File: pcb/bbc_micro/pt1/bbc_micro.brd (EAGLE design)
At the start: 56 x 65 mm, 51 parts, among them IC1 STM32F072C8T6, SW1 324_SW, SW2 324_SW, SW3 324_SW

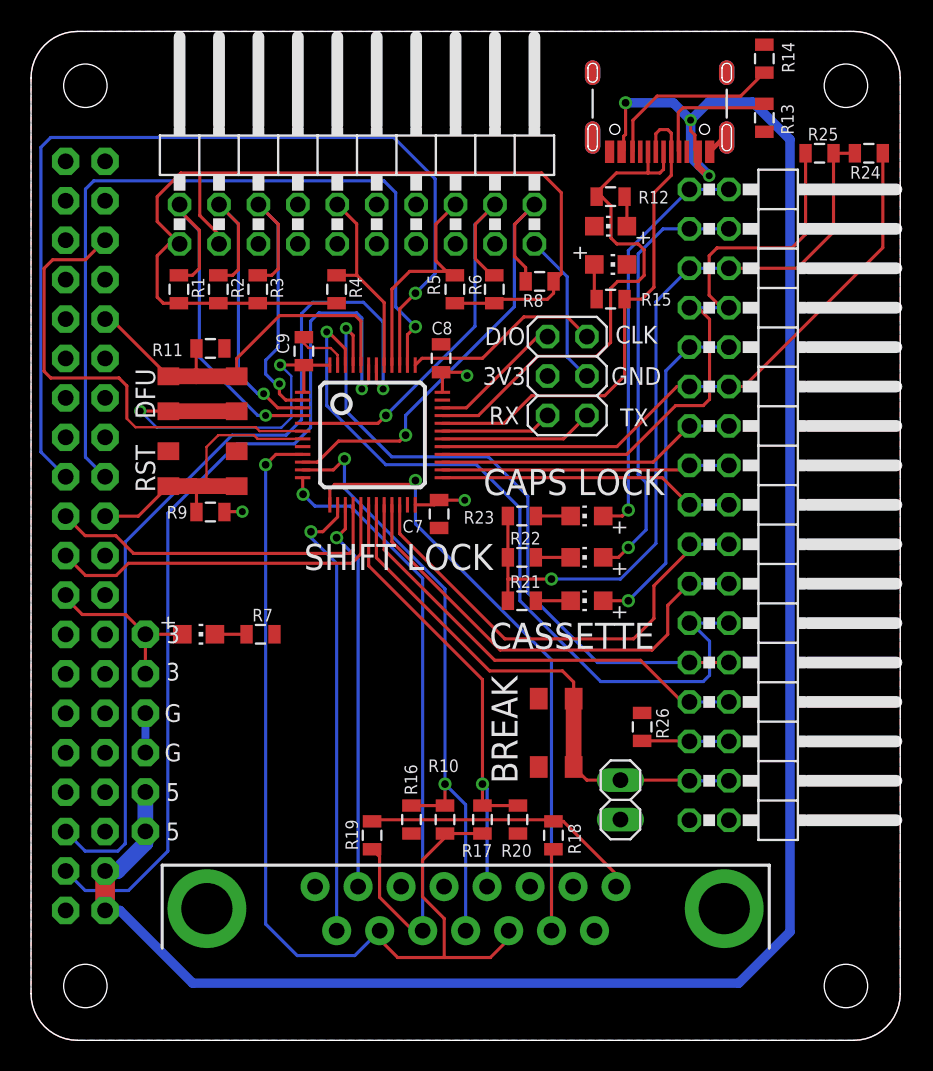
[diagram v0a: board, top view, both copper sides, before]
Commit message: changed to using built-in DAC
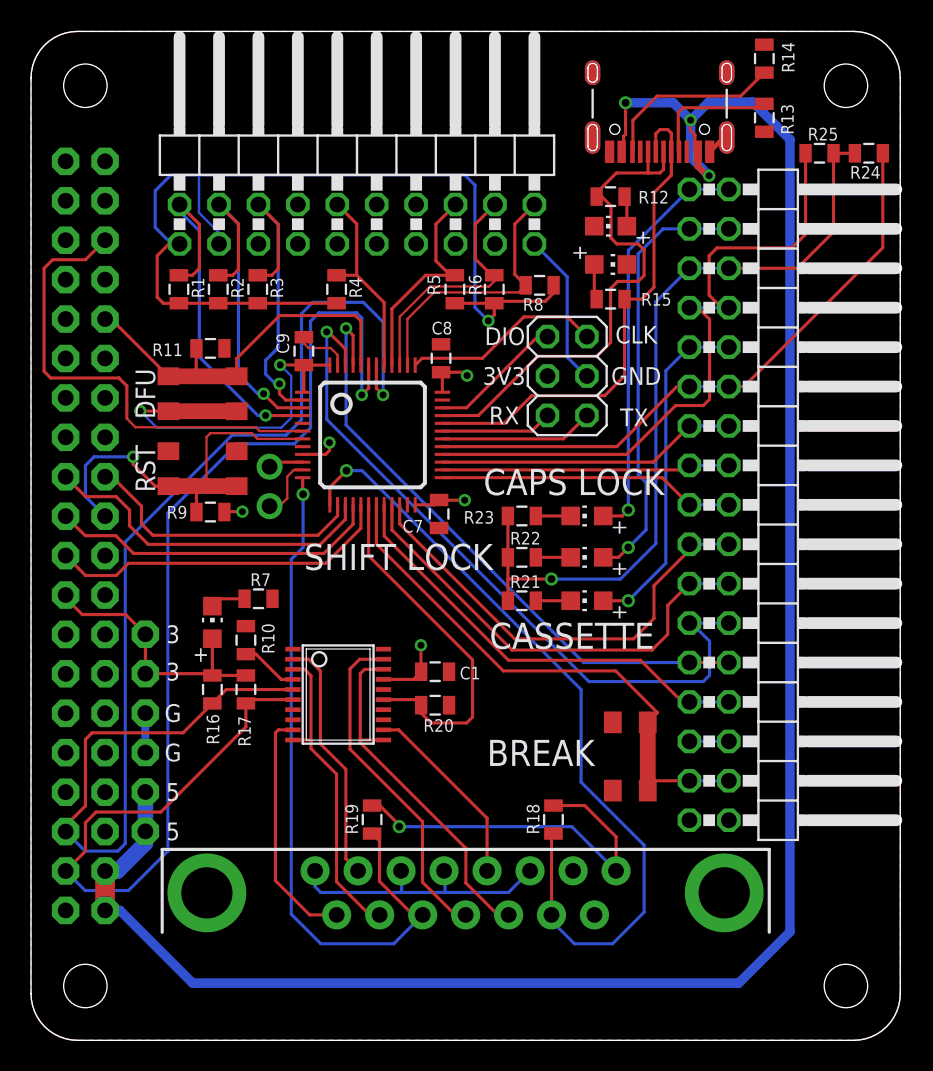
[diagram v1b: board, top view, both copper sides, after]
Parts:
- removed JP5: (no value), pinhead:1X02
- removed R26: 5.1K, SparkFun-Passives:0805
- added C1: 100nF, clock:0805@1
- added U$1: PINHD1X2, adafruit_changed:1X02
- added U$5: MCP4451, ps2:TSSOP20
- R10: value 5.1K -> 2K
- moved R17 17.4 mm to (13.8, 22.6)
- moved R10 17.3 mm to (13.8, 25.8)
- moved R16 15.3 mm to (11.7, 22.6), turned to 90 degrees
- moved R20 9.09 mm to (26.0, 21.6), turned to 0 degrees
- moved SW3 5.01 mm to (38.6, 18.3)
- moved R7 2.29 mm to (14.7, 28.4)
- moved LED1 1.17 mm to (11.7, 26.9), turned to 0 degrees
- moved R18 1.02 mm to (33.7, 14.2)
- moved R19 1.02 mm to (22.0, 14.2)
- moved U$9 1.02 mm to (28.0, 9.50)
- moved R8 0.25 mm to (32.8, 48.6)
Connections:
- removed net N$12 (its old number): IC1.18, R17.2, R20.1, U$9.4
- new net N$10: U$5.19, U$9.12
- new net N$19: U$5.11, U$5.18, U$9.11
- new net N$24: IC1.10, U$1.1
- new net N$25: IC1.18, R20.1, U$5.15
- new net N$31: IC1.11, U$1.2
- new net N$6: U$5.9, U$9.15
- net +3V3: now also C1.2, IC1.9, R16.2, R17.2, U$5.17
- net BREAK: no longer JP5.1
- net CLK: no longer R26.1
- net D6/MIDDLE: now also IC1.39; no longer IC1.5
- net D7/RIGHTT: now also IC1.38; no longer IC1.10
- net GND: now also C1.1, R10.2, U$5.16, U$5.7; no longer JP5.2, R16.2, R26.2
- net N$11: now also U$5.12, U$9.4; no longer IC1.9, R10.1, R17.1, U$9.11, U$9.14
- net N$17: now also U$5.10, U$5.3, U$9.14; no longer IC1.11, R10.2, R16.1, U$9.12
- net N$22: now also R16.1, U$5.5
- net N$23: now also R17.1, U$5.6
- net N$4: now also R10.1, U$5.4; no longer IC1.14, U$9.15
- net N$5: now also U$5.2; no longer IC1.15
- net SPI_CS: now also IC1.14; no longer IC1.38
- net SPI_SCK: now also IC1.15; no longer IC1.39
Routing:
- net N$11: track 63.1 -> 12.4 mm, vias 1 -> 0
- net SPI_SCK: track 61.6 -> 22.0 mm, vias 1 -> 0
- net SPI_CS: track 51.4 -> 18.4 mm, vias 1 -> 0
- net N$12 (its old number): track 31.4 -> 0.00 mm, vias 1 -> 0
- net N$4: track 29.3 -> 3.70 mm, vias 1 -> 0
- net N$25: track 0.00 -> 23.3 mm
- net N$19: track 0.00 -> 23.0 mm
- net N$23: track 58.2 -> 80.1 mm
- net N$22: track 57.6 -> 79.5 mm
- net N$10: track 0.00 -> 21.7 mm
- net N$17: track 40.2 -> 20.1 mm, vias 2 -> 0
- net GND: track 17.5 -> 35.9 mm
- net N$6: track 0.00 -> 15.6 mm
- net D7/RIGHTT: track 31.4 -> 17.5 mm, vias 1 -> 0
- net +3V3: track 44.1 -> 57.3 mm, vias 5 -> 7
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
